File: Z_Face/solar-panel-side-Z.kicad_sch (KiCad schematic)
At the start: 30 parts, among them J1 CON-5040500591, J10 Face0, J11 Face1, J12 Face2, J13 Face3, J4 Conn_01x01, J5 Conn_01x01, J6 Conn_01x01, J7 Conn_01x01, U1 VEML7700, U2 DRV2605LDGS, U3 MCP9808_DFN

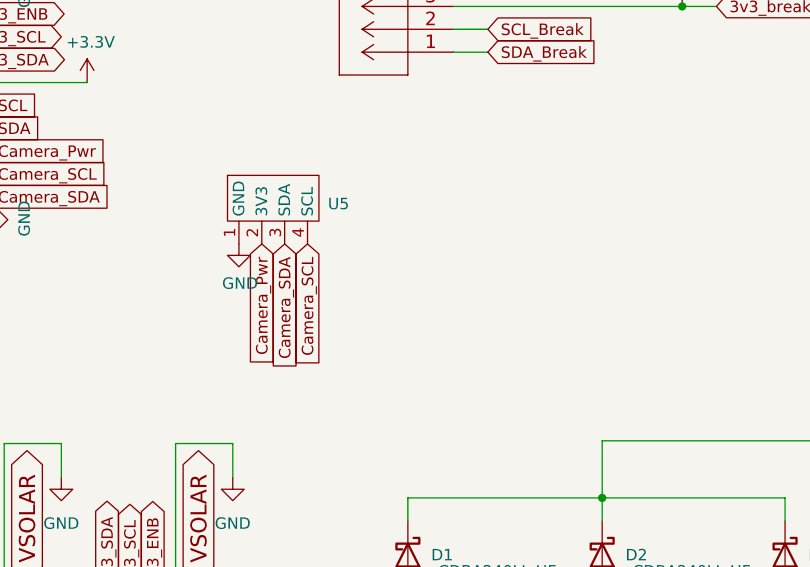
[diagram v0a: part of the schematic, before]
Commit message: added extra pin to z face
moved it slightly closer also
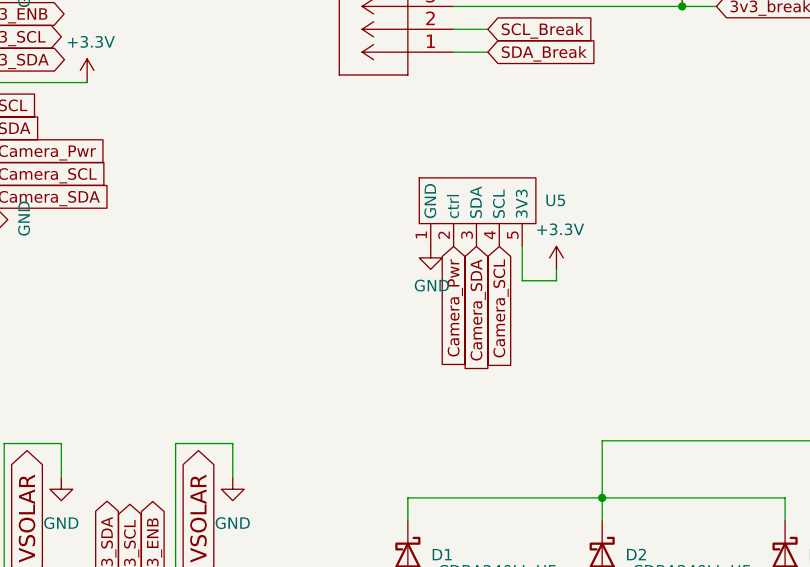
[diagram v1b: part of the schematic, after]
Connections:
- net +3V3: now also U5.5 (3V3)
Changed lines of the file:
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@@
+    (stroke (width 0) (type default))
+  )
+  (wire (pts (xy 189.23 60.96) (xy 189.23 64.77))
     (stroke (width 0) (type default))
   )
@@
     (stroke (width 0) (type default))
   )
+  (wire (pts (xy 193.04 64.77) (xy 193.04 63.5))
+    (stroke (width 0) (type default))
+  )
   (wire (pts (xy 31.75 146.05) (xy 31.75 148.59))
     (stroke (width 0) (type default))
@@
     (stroke (width 0) (type default))
   )
+  (wire (pts (xy 189.23 64.77) (xy 193.04 64.77))
+    (stroke (width 0) (type default))
+  )
   (wire (pts (xy 131.6736 98.0948) (xy 131.6736 82.8548))
     (stroke (width 0) (type default))
@@
     (property "Intersheetrefs" "${INTERSHEET_REFS}" (at 93.653 88.6665 90)
       (effects (font (size 1.27 1.27)) (justify left) hide)
+    )
+  )
+  (global_label "Camera_SDA" (shape input) (at 184.15 60.96 270) (fields_autoplaced)
+    (effects (font (size 1.27 1.27)) (justify right))
+    (property "Intersheetrefs" "${INTERSHEET_REFS}" (at 184.15 74.8834 90)
+      (effects (font (size 1.27 1.27)) (justify right) hide)
     )
   )
@@
     )
   )
-  (global_label "Camera_SDA" (shape input) (at 162.8394 60.6806 270) (fields_autoplaced)
-    (effects (font (size 1.27 1.27)) (justify right))
-    (property "Intersheetrefs" "${INTERSHEET_REFS}" (at 162.8394 74.604 90)
-      (effects (font (size 1.27 1.27)) (justify right) hide)
-    )
-  )
   (global_label "F0_SCL" (shape output) (at 91.0336 98.0948 90) (fields_autoplaced)
     (effects (font (size 1.27 1.27)) (justify left))
@@
     (effects (font (size 1.27 1.27)) (justify right))
     (property "Intersheetrefs" "${INTERSHEET_REFS}" (at 95.0546 55.4482 0)
+      (effects (font (size 1.27 1.27)) (justify right) hide)
+    )
+  )
+  (global_label "Camera_SCL" (shape input) (at 186.69 60.96 270) (fields_autoplaced)
+    (effects (font (size 1.27 1.27)) (justify right))
+    (property "Intersheetrefs" "${INTERSHEET_REFS}" (at 186.69 74.8229 90)
       (effects (font (size 1.27 1.27)) (justify right) hide)
     )
@@
     )
   )
-  (global_label "Camera_Pwr" (shape input) (at 160.2994 60.6806 270) (fields_autoplaced)
-    (effects (font (size 1.27 1.27)) (justify right))
-    (property "Intersheetrefs" "${INTERSHEET_REFS}" (at 160.2994 74.4226 90)
+  (global_label "Camera_Pwr" (shape input) (at 181.61 60.96 270) (fields_autoplaced)
+    (effects (font (size 1.27 1.27)) (justify right))
+    (property "Intersheetrefs" "${INTERSHEET_REFS}" (at 181.61 74.702 90)
       (effects (font (size 1.27 1.27)) (justify right) hide)
     )
@@
     (effects (font (size 1.27 1.27)) (justify right))
     (property "Intersheetrefs" "${INTERSHEET_REFS}" (at 95.1151 37.6682 0)
-      (effects (font (size 1.27 1.27)) (justify right) hide)
-    )
-  )
-  (global_label "Camera_SCL" (shape input) (at 165.3794 60.6806 270) (fields_autoplaced)
-    (effects (font (size 1.27 1.27)) (justify right))
-    (property "Intersheetrefs" "${INTERSHEET_REFS}" (at 165.3794 74.5435 90)
       (effects (font (size 1.27 1.27)) (justify right) hide)
     )
@@
     )
   )
-  (symbol (lib_id "power:GND") (at 157.7594 60.6806 0) (unit 1)
-    (in_bom yes) (on_board yes) (dnp no)
-    (property "Reference" "#PWR019" (at 157.7594 67.0306 0)
-      (effects (font (size 1.27 1.27)) hide)
-    )
-    (property "Value" "GND" (at 157.8864 65.0748 0)
-      (effects (font (size 1.27 1.27)))
-    )
-    (property "Footprint" "" (at 157.7594 60.6806 0)
-      (effects (font (size 1.27 1.27)) hide)
-    )
-    (property "Datasheet" "" (at 157.7594 60.6806 0)
-      (effects (font (size 1.27 1.27)) hide)
-    )
-    (pin "1")
-    (instances
-      (project "solar-panel-side-Z"
-        (path "/b92e10d4-ef16-4e79-8a94-1185be6812fd"
-          (reference "#PWR019") (unit 1)
+  (symbol (lib_id "solar-panel-side-Z-rescue:+3.3V-power") (at 193.04 63.5 0) (unit 1)
+    (in_bom yes) (on_board yes) (dnp no)
+    (property "Reference" "#PWR021" (at 193.04 67.31 0)
+      (effects (font (size 1.27 1.27)) hide)
+    )
+    (property "Value" "+3.3V" (at 193.421 59.1058 0)
+      (effects (font (size 1.27 1.27)))
+    )
+    (property "Footprint" "" (at 193.04 63.5 0)
+      (effects (font (size 1.27 1.27)) hide)
+    )
+    (property "Datasheet" "" (at 193.04 63.5 0)
+      (effects (font (size 1.27 1.27)) hide)
+    )
+    (pin "1")
+    (instances
+      (project "solar-panel-side-Z"
+        (path "/b92e10d4-ef16-4e79-8a94-1185be6812fd"
+          (reference "#PWR021") (unit 1)
         )
       )
@@
         (path "/b92e10d4-ef16-4e79-8a94-1185be6812fd"
           (reference "#PWR02") (unit 1)
+        )
+      )
+    )
+  )
+  (symbol (lib_id "power:GND") (at 179.07 60.96 0) (unit 1)
+    (in_bom yes) (on_board yes) (dnp no)
+    (property "Reference" "#PWR024" (at 179.07 67.31 0)
+      (effects (font (size 1.27 1.27)) hide)
+    )
+    (property "Value" "GND" (at 179.197 65.3542 0)
+      (effects (font (size 1.27 1.27)))
+    )
+    (property "Footprint" "" (at 179.07 60.96 0)
+      (effects (font (size 1.27 1.27)) hide)
+    )
+    (property "Datasheet" "" (at 179.07 60.96 0)
+      (effects (font (size 1.27 1.27)) hide)
+    )
+    (pin "1")
+    (instances
+      (project "solar-panel-side-Z"
+        (path "/b92e10d4-ef16-4e79-8a94-1185be6812fd"
+          (reference "#PWR024") (unit 1)
         )
       )
@@
         (path "/b92e10d4-ef16-4e79-8a94-1185be6812fd"
           (reference "J8") (unit 1)
-        )
-      )
-    )
-  )
-  (symbol (lib_id "camera_daughter:camera_daughter") (at 161.5694 51.7906 0) (unit 1)
-    (in_bom yes) (on_board yes) (dnp no) (fields_autoplaced)
-    (property "Reference" "U5" (at 167.64 56.2356 0)
-      (effects (font (size 1.27 1.27)) (justify left))
-    )
-    (property "Value" "~" (at 161.5694 51.7906 0)
-      (effects (font (size 1.27 1.27)))
-    )
-    (property "Footprint" "camera_daughter:camera_daughter" (at 161.5694 51.7906 0)
-      (effects (font (size 1.27 1.27)) hide)
-    )
-    (property "Datasheet" "" (at 161.5694 51.7906 0)
-      (effects (font (size 1.27 1.27)) hide)
-    )
-    (pin "1")
-    (pin "2")
-    (pin "3")
-    (pin "4")
-    (instances
-      (project "solar-panel-side-Z"
-        (path "/b92e10d4-ef16-4e79-8a94-1185be6812fd"
-          (reference "U5") (unit 1)
         )
       )
@@
         )
       )
+    )
+  )
+  (symbol (lib_id "camera_daughter:camera_daughter") (at 182.88 52.07 0) (unit 1)
+    (in_bom yes) (on_board yes) (dnp no) (fields_autoplaced)
+    (property "Reference" "U5" (at 191.77 55.88 0)
+      (effects (font (size 1.27 1.27)) (justify left))
+    )
+    (property "Value" "~" (at 182.88 52.07 0)
+      (effects (font (size 1.27 1.27)))
+    )
+    (property "Footprint" "camera_daughter:camera_daughter" (at 182.88 52.07 0)
+      (effects (font (size 1.27 1.27)) hide)
+    )
+    (property "Datasheet" "" (at 182.88 52.07 0)
+      (effects (font (size 1.27 1.27)) hide)
+    )
+    (pin "1")
+    (pin "2")
+    (pin "3")
+    (pin "4")
+    (pin "5")
+    (instances
+      (project "solar-panel-side-Z"
+        (path "/b92e10d4-ef16-4e79-8a94-1185be6812fd"
+          (reference "U5") (unit 1)
+        )
+      )
